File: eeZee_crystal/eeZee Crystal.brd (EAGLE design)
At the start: 8.9 x 9.5 mm, 4 parts, among them Q1 16MHz

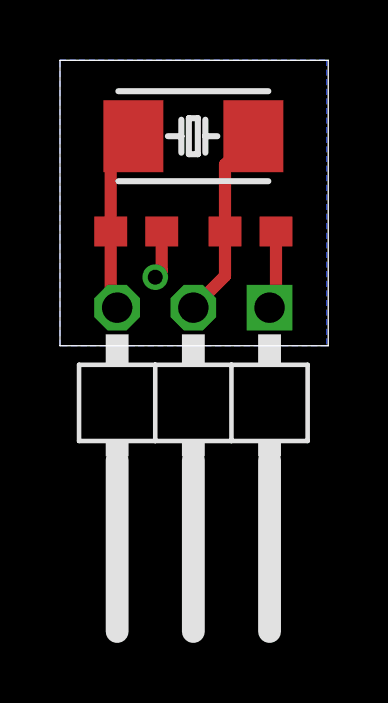
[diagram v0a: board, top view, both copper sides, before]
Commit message: Changed 3-pin header to vertical style (displays better in Eagle)
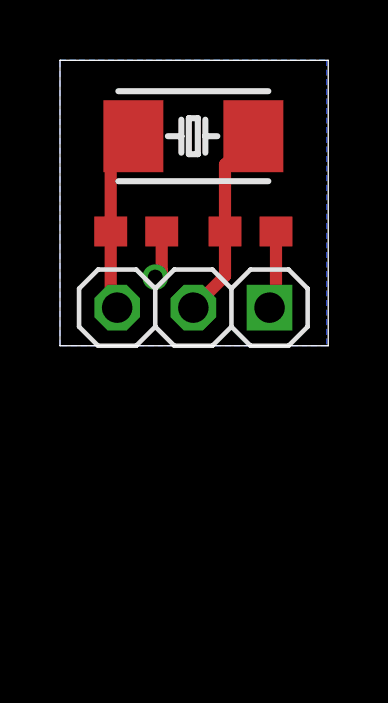
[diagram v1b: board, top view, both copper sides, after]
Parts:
- JP1: device pinhead-2:1X03/90-S -> pinhead-2:1X03-S
- moved JP1 3.81 mm to (4.45, 1.27)

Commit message: Resized board narrower and aligned to inches. Added silk for multiple frequencies. Mitred corners. Changed silk print sizes.
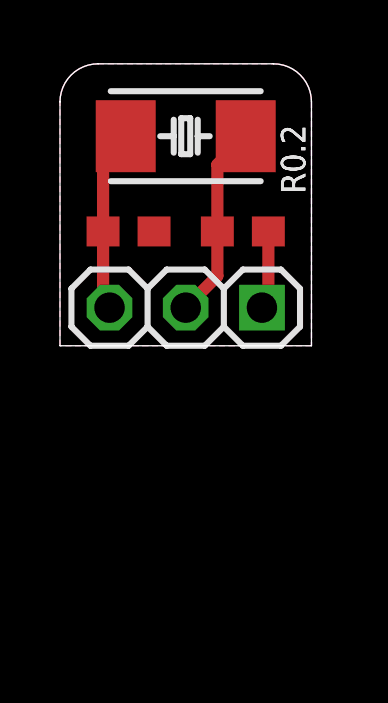
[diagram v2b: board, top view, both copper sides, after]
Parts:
- Q1: value 16MHz -> (none)
- moved JP1 0.25 mm to (4.19, 1.27)
- moved Q1 0.25 mm to (4.19, 6.99)
- moved C2 0.25 mm to (2.29, 3.81)
- moved C1 0.25 mm to (6.10, 3.81)
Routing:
- net GND: track 4.24 -> 2.63 mm, vias 1 -> 0
- added copper zone on layer 1, net GND
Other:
- board size 8.9 x 9.5 mm -> 8.4 x 9.4 mm
- board text added: "10"
- board text added: "12"
- board text added: "16"
- board text added: "8"
- board text added: "MHz"
- board text added: "R0.2"
- board text removed: "16MHz"

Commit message: Increaed spacing to 8/10mil for most objects, reduced distance to 10mil.
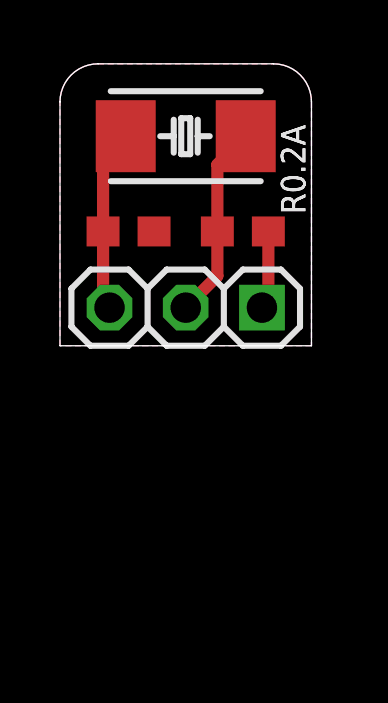
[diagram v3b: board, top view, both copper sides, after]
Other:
- board text added: "R0.2A"
- board text removed: "R0.2"
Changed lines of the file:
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@@
 <layer number="19" name="Unrouted" color="6" fill="1" visible="yes" active="yes"/>
 <layer number="20" name="Dimension" color="15" fill="1" visible="yes" active="yes"/>
-<layer number="21" name="tPlace" color="7" fill="1" visible="no" active="yes"/>
-<layer number="22" name="bPlace" color="7" fill="1" visible="no" active="yes"/>
-<layer number="23" name="tOrigins" color="15" fill="1" visible="no" active="yes"/>
-<layer number="24" name="bOrigins" color="15" fill="1" visible="no" active="yes"/>
-<layer number="25" name="tNames" color="7" fill="1" visible="no" active="yes"/>
+<layer number="21" name="tPlace" color="7" fill="1" visible="yes" active="yes"/>
+<layer number="22" name="bPlace" color="7" fill="1" visible="yes" active="yes"/>
+<layer number="23" name="tOrigins" color="15" fill="1" visible="yes" active="yes"/>
+<layer number="24" name="bOrigins" color="15" fill="1" visible="yes" active="yes"/>
+<layer number="25" name="tNames" color="7" fill="1" visible="yes" active="yes"/>
 <layer number="26" name="bNames" color="7" fill="1" visible="yes" active="yes"/>
-<layer number="27" name="tValues" color="7" fill="1" visible="no" active="yes"/>
-<layer number="28" name="bValues" color="7" fill="1" visible="no" active="yes"/>
+<layer number="27" name="tValues" color="7" fill="1" visible="yes" active="yes"/>
+<layer number="28" name="bValues" color="7" fill="1" visible="yes" active="yes"/>
 <layer number="29" name="tStop" color="7" fill="3" visible="yes" active="yes"/>
 <layer number="30" name="bStop" color="7" fill="6" visible="yes" active="yes"/>
@@
 <rectangle x1="3.683" y1="8.128" x2="4.699" y2="9.144" layer="26"/>
 <text x="5.08" y="5.588" size="1.016" layer="26" font="vector" ratio="12" rot="MR90">MHz</text>
-<text x="7.366" y="7.366" size="0.8128" layer="25" font="vector" ratio="12" rot="R270">R0.2</text>
+<text x="7.366" y="7.366" size="0.8128" layer="25" font="vector" ratio="12" rot="R270">R0.2A</text>
 <wire x1="7.366" y1="0" x2="6.096" y2="0" width="0.2032" layer="121"/>
 <wire x1="6.096" y1="0" x2="5.461" y2="0.635" width="0.2032" layer="121"/>
@@
 <text x="3.81" y="2.413" size="1.016" layer="122" font="vector" ratio="20" rot="MR90">X1</text>
 <text x="1.143" y="2.413" size="1.016" layer="122" font="vector" ratio="20" rot="MR90">X2</text>
-<text x="7.366" y="7.366" size="0.8128" layer="121" font="vector" ratio="25" rot="R270">R0.2</text>
+<text x="7.366" y="7.366" size="0.8128" layer="121" font="vector" ratio="25" rot="R270">R0.2A</text>
 <text x="3.175" y="4.318" size="1.016" layer="122" font="vector" ratio="20" rot="MR0">8</text>
 <text x="3.175" y="5.588" size="1.016" layer="122" font="vector" ratio="20" rot="MR0">10</text>
@@
 <param name="mtCopper" value="0.0356mm 0.0356mm 0.0356mm 0.0356mm 0.0356mm 0.0356mm 0.0356mm 0.0356mm 0.0356mm 0.0356mm 0.0356mm 0.0356mm 0.0356mm 0.0356mm 0.0356mm 0.0356mm"/>
 <param name="mtIsolate" value="1.5011mm 0.1499mm 0.2007mm 0.1499mm 0.2007mm 0.1499mm 0.2007mm 0.1499mm 0.2007mm 0.1499mm 0.2007mm 0.1499mm 0.2007mm 0.1499mm 0.2007mm"/>
-<param name="mdWireWire" value="6mil"/>
-<param name="mdWirePad" value="6mil"/>
-<param name="mdWireVia" value="6mil"/>
-<param name="mdPadPad" value="6mil"/>
-<param name="mdPadVia" value="6mil"/>
-<param name="mdViaVia" value="6mil"/>
+<param name="mdWireWire" value="10mil"/>
+<param name="mdWirePad" value="10mil"/>
+<param name="mdWireVia" value="10mil"/>
+<param name="mdPadPad" value="10mil"/>
+<param name="mdPadVia" value="10mil"/>
+<param name="mdViaVia" value="10mil"/>
 <param name="mdSmdPad" value="0mil"/>
 <param name="mdSmdVia" value="0mil"/>
-<param name="mdSmdSmd" value="6mil"/>
+<param name="mdSmdSmd" value="8mil"/>
 <param name="mdViaViaSameLayer" value="8mil"/>
 <param name="mnLayersViaInSmd" value="2"/>
-<param name="mdCopperDimension" value="15mil"/>
-<param name="mdDrill" value="6mil"/>
+<param name="mdCopperDimension" value="10mil"/>
+<param name="mdDrill" value="10mil"/>
 <param name="mdSmdStop" value="0mil"/>
 <param name="msWidth" value="6mil"/>

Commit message: Modified schematic for easier reading, added letter box. Added 20MHz option to board.
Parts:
- C1, C2: value 8pF -> 12pF
- Q1: value (none) -> 8-20MHz
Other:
- board text added: "20"
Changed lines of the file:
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@@
 <layer number="19" name="Unrouted" color="6" fill="1" visible="yes" active="yes"/>
 <layer number="20" name="Dimension" color="15" fill="1" visible="yes" active="yes"/>
-<layer number="21" name="tPlace" color="7" fill="1" visible="yes" active="yes"/>
-<layer number="22" name="bPlace" color="7" fill="1" visible="yes" active="yes"/>
-<layer number="23" name="tOrigins" color="15" fill="1" visible="yes" active="yes"/>
-<layer number="24" name="bOrigins" color="15" fill="1" visible="yes" active="yes"/>
-<layer number="25" name="tNames" color="7" fill="1" visible="yes" active="yes"/>
-<layer number="26" name="bNames" color="7" fill="1" visible="yes" active="yes"/>
-<layer number="27" name="tValues" color="7" fill="1" visible="yes" active="yes"/>
-<layer number="28" name="bValues" color="7" fill="1" visible="yes" active="yes"/>
+<layer number="21" name="tPlace" color="7" fill="1" visible="no" active="yes"/>
+<layer number="22" name="bPlace" color="7" fill="1" visible="no" active="yes"/>
+<layer number="23" name="tOrigins" color="15" fill="1" visible="no" active="yes"/>
+<layer number="24" name="bOrigins" color="15" fill="1" visible="no" active="yes"/>
+<layer number="25" name="tNames" color="7" fill="1" visible="no" active="yes"/>
+<layer number="26" name="bNames" color="7" fill="1" visible="no" active="yes"/>
+<layer number="27" name="tValues" color="7" fill="1" visible="no" active="yes"/>
+<layer number="28" name="bValues" color="7" fill="1" visible="no" active="yes"/>
 <layer number="29" name="tStop" color="7" fill="3" visible="yes" active="yes"/>
 <layer number="30" name="bStop" color="7" fill="6" visible="yes" active="yes"/>
@@
 <wire x1="0" y1="8.128" x2="0" y2="0" width="0" layer="20"/>
 <text x="6.223" y="2.413" size="1.016" layer="22" font="vector" rot="MR90">GND</text>
-<text x="3.81" y="2.413" size="1.016" layer="22" font="vector" rot="MR90">X1</text>
-<text x="1.143" y="2.413" size="1.016" layer="22" font="vector" rot="MR90">X2</text>
-<text x="3.175" y="4.318" size="1.016" layer="26" font="vector" ratio="12" rot="MR0">8</text>
-<text x="3.175" y="5.588" size="1.016" layer="26" font="vector" ratio="12" rot="MR0">10</text>
-<text x="3.175" y="6.858" size="1.016" layer="26" font="vector" ratio="12" rot="MR0">12</text>
-<text x="3.175" y="8.128" size="1.016" layer="26" font="vector" ratio="12" rot="MR0">16</text>
-<rectangle x1="3.683" y1="4.318" x2="4.699" y2="5.334" layer="26"/>
-<rectangle x1="3.683" y1="5.588" x2="4.699" y2="6.604" layer="26"/>
-<rectangle x1="3.683" y1="6.858" x2="4.699" y2="7.874" layer="26"/>
-<rectangle x1="3.683" y1="8.128" x2="4.699" y2="9.144" layer="26"/>
-<text x="5.08" y="5.588" size="1.016" layer="26" font="vector" ratio="12" rot="MR90">MHz</text>
+<text x="4.953" y="2.54" size="1.016" layer="22" font="vector" rot="MR0">X1</text>
+<text x="2.413" y="2.413" size="1.016" layer="22" font="vector" rot="MR0">X2</text>
+<text x="2.159" y="6.858" size="1.016" layer="26" font="vector" ratio="12" rot="MR0">8</text>
+<text x="2.159" y="5.588" size="1.016" layer="26" font="vector" ratio="12" rot="MR0">10</text>
+<text x="2.159" y="4.318" size="1.016" layer="26" font="vector" ratio="12" rot="MR0">12</text>
+<text x="5.969" y="6.858" size="1.016" layer="26" font="vector" ratio="12" rot="MR0">16</text>
+<rectangle x1="2.413" y1="5.588" x2="3.429" y2="6.604" layer="26"/>
+<rectangle x1="2.413" y1="4.318" x2="3.429" y2="5.334" layer="26"/>
+<rectangle x1="2.413" y1="6.858" x2="3.429" y2="7.874" layer="26"/>
+<text x="5.334" y="8.128" size="1.016" layer="26" font="vector" ratio="12" rot="MR0">MHz</text>
 <text x="7.366" y="7.366" size="0.8128" layer="25" font="vector" ratio="12" rot="R270">R0.2A</text>
+<rectangle x1="6.223" y1="6.858" x2="7.239" y2="7.874" layer="26"/>
+<rectangle x1="6.223" y1="5.588" x2="7.239" y2="6.604" layer="26"/>
+<text x="5.969" y="5.588" size="1.016" layer="26" font="vector" ratio="12" rot="MR0">20</text>
 <wire x1="7.366" y1="0" x2="6.096" y2="0" width="0.2032" layer="121"/>
 <wire x1="6.096" y1="0" x2="5.461" y2="0.635" width="0.2032" layer="121"/>
@@
 <wire x1="4.0409875" y1="6.385" x2="4.0409875" y2="7.585" width="0.2032" layer="121"/>
 <text x="6.223" y="2.413" size="1.016" layer="122" font="vector" ratio="20" rot="MR90">GND</text>
-<text x="3.81" y="2.413" size="1.016" layer="122" font="vector" ratio="20" rot="MR90">X1</text>
-<text x="1.143" y="2.413" size="1.016" layer="122" font="vector" ratio="20" rot="MR90">X2</text>
+<text x="4.953" y="2.54" size="1.016" layer="122" font="vector" ratio="20" rot="MR0">X1</text>
+<text x="2.413" y="2.413" size="1.016" layer="122" font="vector" ratio="20" rot="MR0">X2</text>
 <text x="7.366" y="7.366" size="0.8128" layer="121" font="vector" ratio="25" rot="R270">R0.2A</text>
-<text x="3.175" y="4.318" size="1.016" layer="122" font="vector" ratio="20" rot="MR0">8</text>
-<text x="3.175" y="5.588" size="1.016" layer="122" font="vector" ratio="20" rot="MR0">10</text>
-<text x="3.175" y="6.858" size="1.016" layer="122" font="vector" ratio="20" rot="MR0">12</text>
-<text x="3.175" y="8.128" size="1.016" layer="122" font="vector" ratio="20" rot="MR0">16</text>
-<text x="5.08" y="5.588" size="1.016" layer="122" font="vector" ratio="20" rot="MR90">MHz</text>
-<rectangle x1="3.683" y1="8.128" x2="4.699" y2="9.144" layer="122"/>
-<rectangle x1="3.683" y1="6.858" x2="4.699" y2="7.874" layer="122"/>
-<rectangle x1="3.683" y1="5.588" x2="4.699" y2="6.604" layer="122"/>
-<rectangle x1="3.683" y1="4.318" x2="4.699" y2="5.334" layer="122"/>
+<text x="2.159" y="6.858" size="1.016" layer="122" font="vector" ratio="20" rot="MR0">8</text>
+<text x="2.159" y="5.588" size="1.016" layer="122" font="vector" ratio="20" rot="MR0">10</text>
+<text x="2.159" y="4.318" size="1.016" layer="122" font="vector" ratio="20" rot="MR0">12</text>
+<text x="5.969" y="6.858" size="1.016" layer="122" font="vector" ratio="20" rot="MR0">16</text>
+<text x="5.334" y="8.128" size="1.016" layer="122" font="vector" ratio="20" rot="MR0">MHz</text>
+<text x="5.969" y="5.588" size="1.016" layer="122" font="vector" ratio="20" rot="MR0">20</text>
+<rectangle x1="2.413" y1="5.588" x2="3.429" y2="6.604" layer="122"/>
+<rectangle x1="2.413" y1="4.318" x2="3.429" y2="5.334" layer="122"/>
+<rectangle x1="2.413" y1="6.858" x2="3.429" y2="7.874" layer="122"/>
+<rectangle x1="6.223" y1="6.858" x2="7.239" y2="7.874" layer="122"/>
+<rectangle x1="6.223" y1="5.588" x2="7.239" y2="6.604" layer="122"/>
 </plain>
 <attributes>
@@
 </autorouter>
 <elements>
-<element name="Q1" library="mes_crystal" package="NDK_2PAD_5X3" value="" x="4.191" y="6.985" smashed="yes">
+<element name="Q1" library="mes_crystal" package="NDK_2PAD_5X3" value="8-20MHz" x="4.191" y="6.985" smashed="yes">
 <attribute name="PARTNO" value="NX5032GA-16.000000MHZ-LN-CD-1" x="4.191" y="6.985" size="1.778" layer="27" display="off"/>
 <attribute name="VALUE" x="0.202" y="9.196" size="1.016" layer="28" font="vector" ratio="12" rot="MR180"/>
+<attribute name="LOAD" value="12pF" x="4.191" y="6.985" size="1.778" layer="27" display="off"/>
 </element>
-<element name="C1" library="rcl" package="C0603" value="8pF" x="6.096" y="3.81" smashed="yes">
+<element name="C1" library="rcl" package="C0603" value="12pF" x="6.096" y="3.81" smashed="yes">
 <attribute name="PARTNO" value="C1608C0G1H080D" x="6.096" y="3.81" size="1.778" layer="27" display="off"/>
 <attribute name="BOM" value="INCLUDE" x="6.096" y="3.81" size="1.778" layer="27" display="off"/>
 </element>
-<element name="C2" library="rcl" package="C0603" value="8pF" x="2.286" y="3.81" smashed="yes">
+<element name="C2" library="rcl" package="C0603" value="12pF" x="2.286" y="3.81" smashed="yes">
 <attribute name="PARTNO" value="C1608C0G1H080D" x="2.286" y="3.81" size="1.778" layer="27" display="off"/>
 <attribute name="BOM" value="INCLUDE" x="2.286" y="3.81" size="1.778" layer="27" display="off"/>
